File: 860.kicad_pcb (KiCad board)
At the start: 4 copper layers, 38 x 106 mm, 150 parts, among them J1 PJ301B, J2 PJ301B, J3 PJ301B, J4 PJ301B, J5 PJ301B, J6 PJ301B, P1 CONN_02X05, Q1 BCM857BS, Q2 BCM857BS, Q3 J112, Q4 J112, Q5 J112, Q6 J112, SW1 B3F-1050, U1 TL072-, U10 CD4027, U11 CD40106, U12 TS321, U13 TS321, U2 TL072-, U3 TL072-, U4 TL072-, U5 LM13700, U6 LM13700, U7 LM13700, U8 DG409, U9 CD4052

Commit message: routed, silk screen adjusted
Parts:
- C18, C25, C6, C7: footprint MyModules:SM0805-HAND -> MyModules:SM0805-HAND-C
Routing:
- net GND: track 88.8 -> 92.7 mm, vias 24 -> 26
- net Net-(J4-Pad3): track 32.3 -> 35.5 mm
- net Net-(U1-Pad5): track 43.1 -> 45.9 mm
- net Net-(U10-Pad1): track 72.7 -> 75.2 mm
- net Net-(Q3-Pad1): track 55.1 -> 53.7 mm
- net Net-(R48-Pad1): track 26.9 -> 28.0 mm
- net Net-(J1-Pad3): track 35.0 -> 34.0 mm
- net -12V: track 290.8 -> 291.7 mm
- net Net-(C11-Pad1): track 54.5 -> 55.3 mm
- net Net-(R31-Pad1): track 2.08 -> 2.60 mm
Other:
- rule pad_to_mask_clearance: 0.2 -> 0.05

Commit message: getting pretty close to done
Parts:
- added G***: LOGO, LOGO, B.Cu at (122.2, 127.8)
- added REF***: OSHW-Symbol_6.7x6mm_SilkScreen, Symbols:OSHW-Symbol_6.7x6mm_SilkScreen, B.Cu at (135.4, 41.9)
- moved D6 0.20 mm to (121.3, 106.5)
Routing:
- net -12V: vias 17 -> 16
- added copper zone on B.Cu, net -12V
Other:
- board text added: "860"
- board text added: "FREQ"
- board text added: "RES"
- board text added: "r1 11/17"
- board text added: "system80.net"

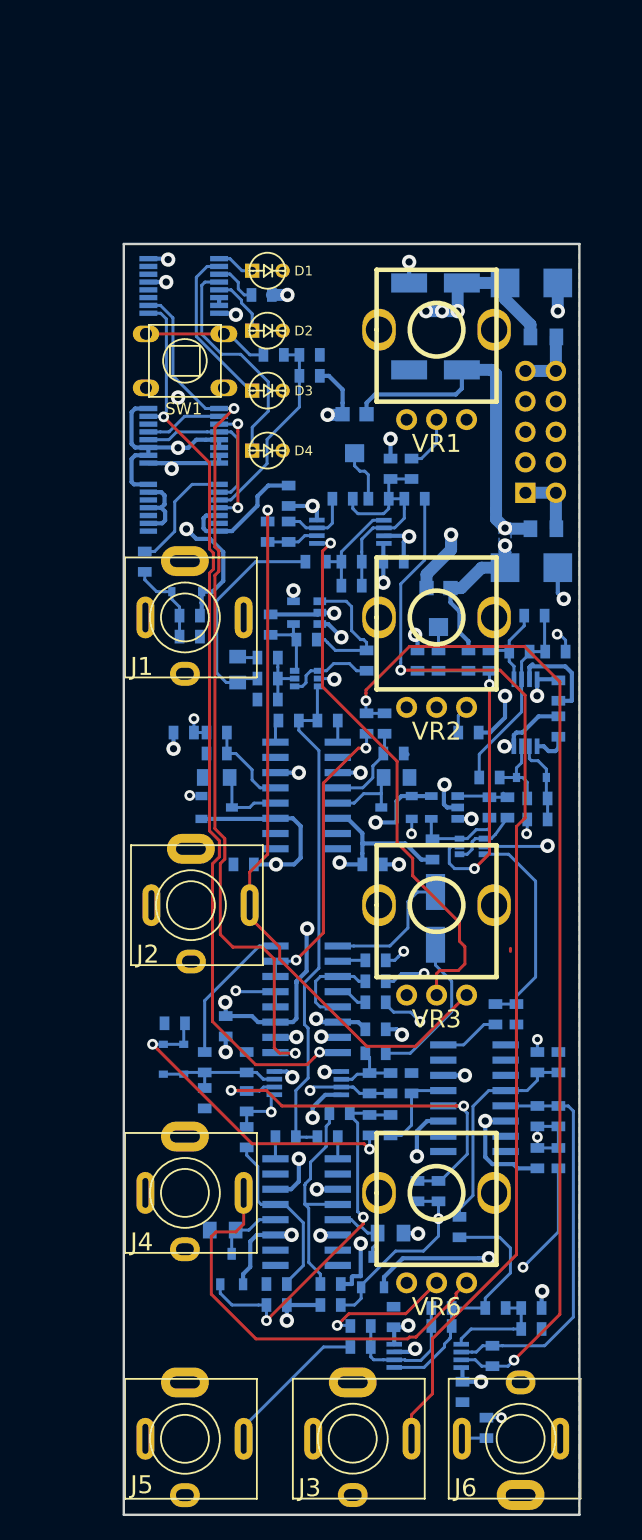
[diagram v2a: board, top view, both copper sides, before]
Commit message: front component adjustments to jive with panel template
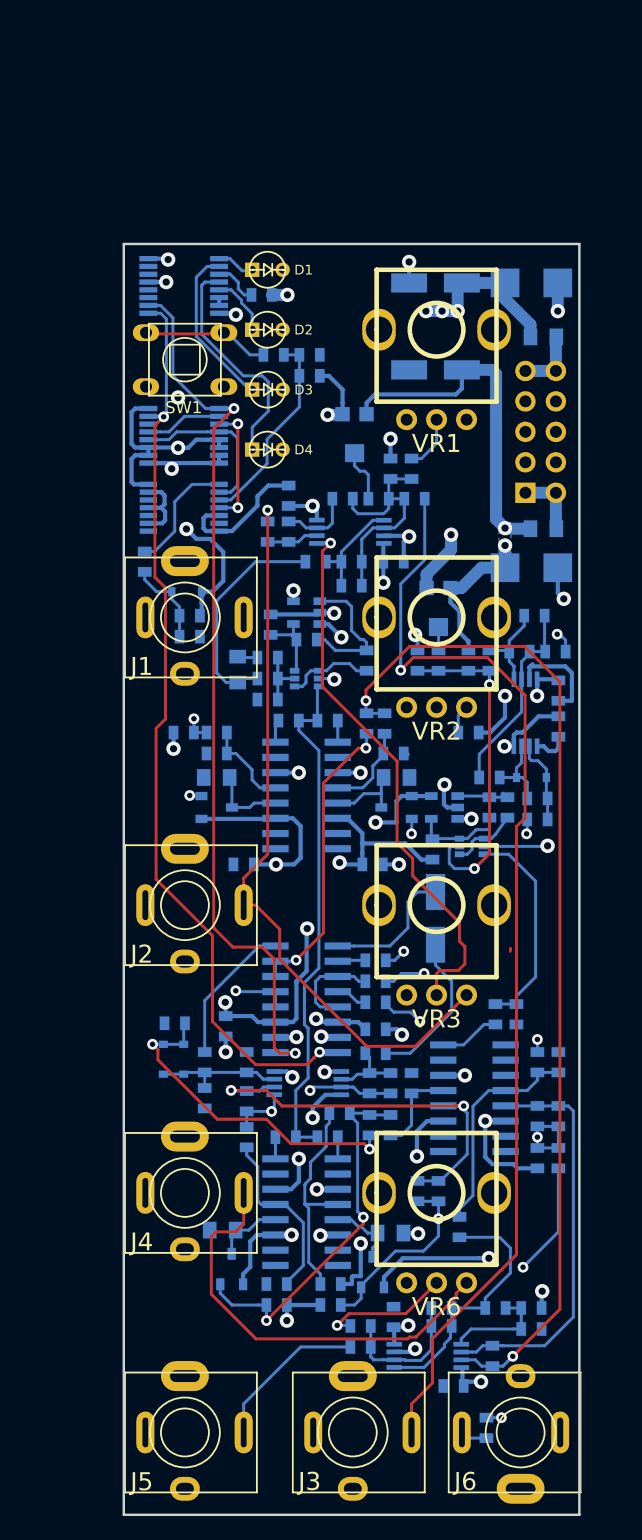
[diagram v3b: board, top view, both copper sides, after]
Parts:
- moved C14 0.90 mm to (145.5, 133.8), turned to 180 degrees
- moved J5 0.53 mm to (123.1, 137.6)
- moved J3 0.52 mm to (137.1, 137.6)
- moved J6 0.52 mm to (151.1, 137.6)
- moved J2 0.50 mm to (123.1, 93.7)
- moved SW1 0.10 mm to (123.1, 48.1)
- moved D1 0.08 mm to (130.0, 40.6)
- moved D2 0.08 mm to (130.0, 45.6)
- moved D3 0.08 mm to (130.0, 50.6)
- moved D4 0.08 mm to (130.0, 55.6)
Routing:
- net Net-(J2-Pad3): track 60.4 -> 62.4 mm
- net Net-(J5-Pad3): track 12.7 -> 13.8 mm
- net Net-(J3-Pad3): track 92.3 -> 93.2 mm
- net -12V: track 291.7 -> 292.4 mm
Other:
- board text added: "-12V"
- board text added: "r1.1 02/18"
- board text removed: "r1 11/17"

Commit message: tweaked routing to improve ground plane
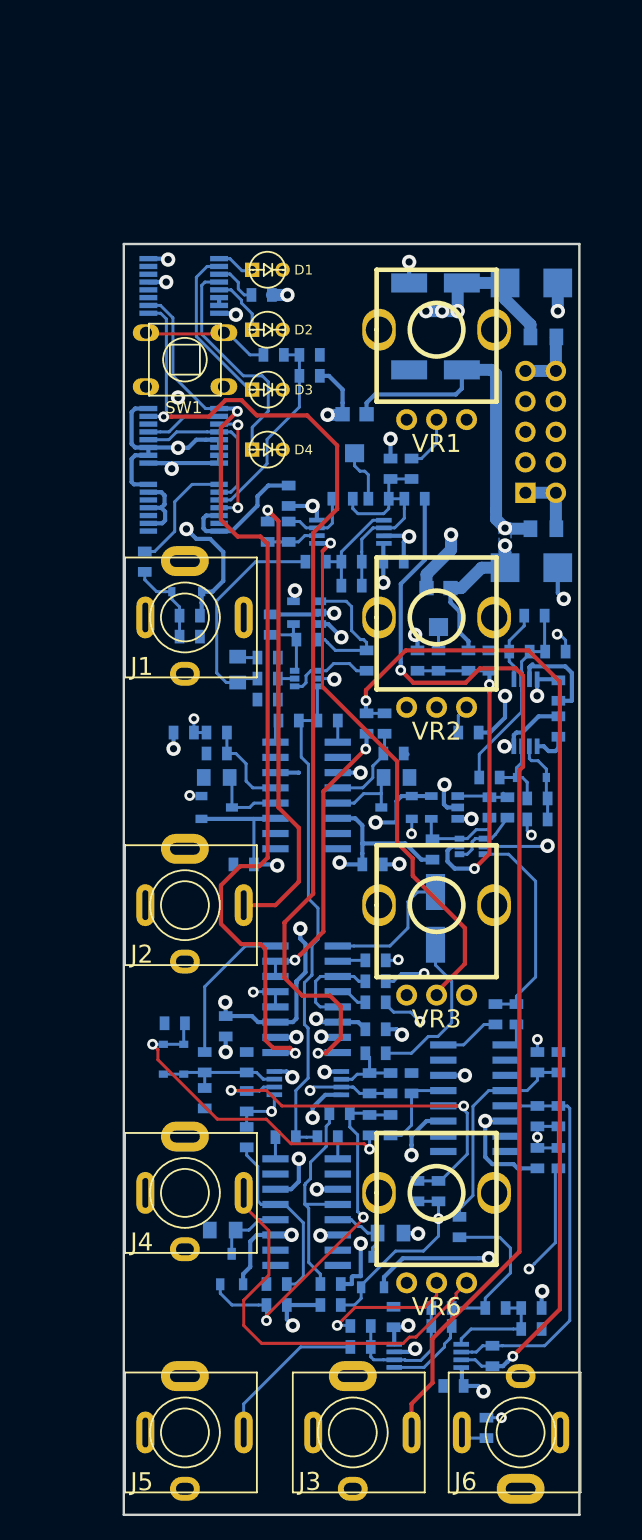
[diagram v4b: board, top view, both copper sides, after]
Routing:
- net Net-(U10-Pad15): track 77.0 -> 86.5 mm
- net Net-(U10-Pad1): track 74.7 -> 79.3 mm
- net -12V: track 292.4 -> 294.7 mm
- net Net-(J1-Pad3): track 34.0 -> 36.0 mm
- net +12V: track 352.8 -> 354.8 mm
- net OUT2A: track 58.8 -> 57.1 mm
- net Net-(R48-Pad1): track 27.8 -> 26.3 mm
- net Net-(J4-Pad3): track 35.5 -> 34.3 mm
- net Net-(U1-Pad5): track 45.9 -> 45.0 mm
- net Net-(J3-Pad3): track 93.2 -> 94.0 mm
- net SWX1: track 12.1 -> 12.8 mm
- net Net-(R7-Pad2): track 10.9 -> 11.5 mm
- net Net-(C10-Pad1): track 13.1 -> 13.6 mm
- net GND: vias 26 -> 25

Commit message: fixed hardware placement to match panel mechanical, moving power header
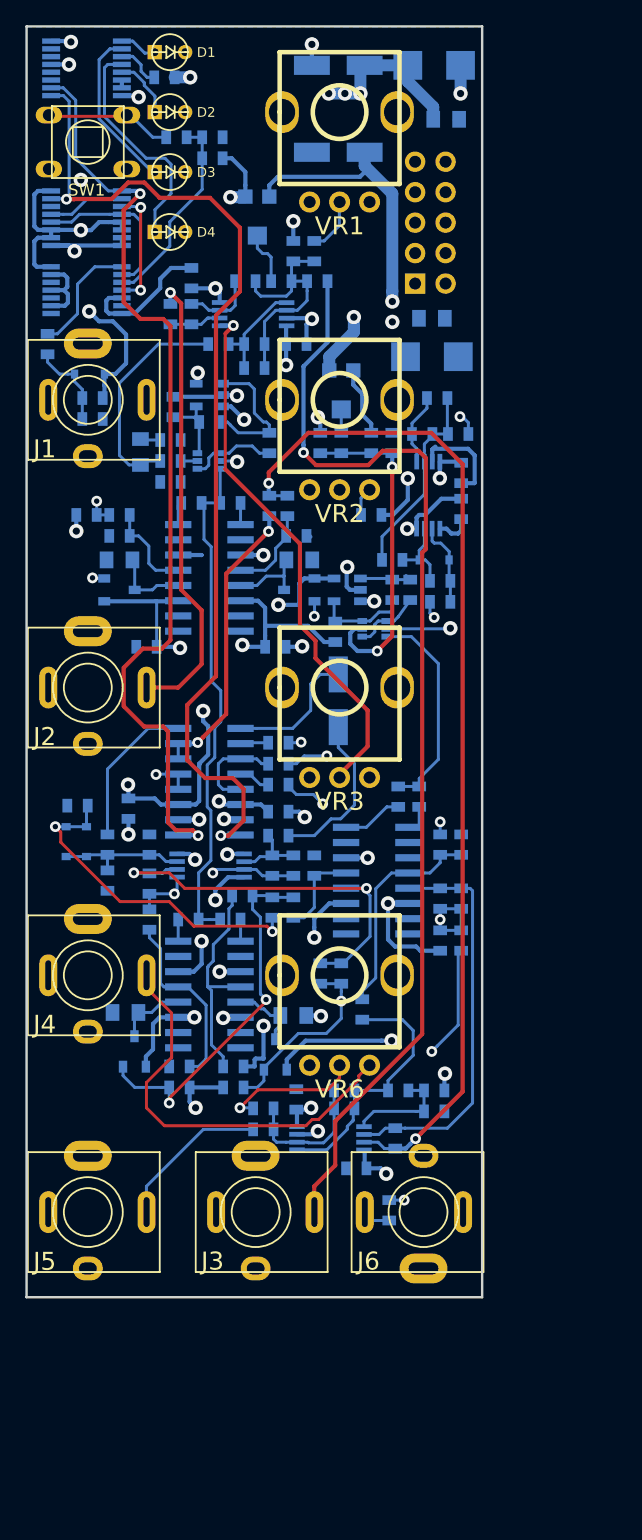
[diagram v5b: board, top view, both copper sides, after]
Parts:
- moved J3 20.1 mm to (129.0, 119.2)
- moved J5 20.1 mm to (115.0, 119.2)
- moved J6 20.1 mm to (143.0, 119.2)
- moved D1 19.9 mm to (121.8, 22.5)
- moved D2 19.9 mm to (121.8, 27.5)
- moved D3 19.9 mm to (121.8, 32.5)
- moved D4 19.9 mm to (121.8, 37.5)
- moved C1 19.9 mm to (136.4, 110.6)
- moved C10 19.9 mm to (135.9, 76.6)
- moved C11 19.9 mm to (132.1, 90.3)
- moved C14 19.9 mm to (137.4, 115.6)
- moved C15 19.9 mm to (132.4, 109.8)
- moved C19 19.9 mm to (130.9, 85.8)
- moved C2 19.9 mm to (140.4, 67.3)
- moved C25 19.9 mm to (132.1, 102.8)
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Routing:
- net -12V: track 294.7 -> 282.3 mm
- net Net-(F1-Pad2): track 5.56 -> 0.00 mm
- net Net-(F2-Pad2): track 5.40 -> 0.06 mm
- net GND: track 92.7 -> 89.9 mm, vias 25 -> 24
- removed copper zone on B.Cu, net -12V
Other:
- board text added: "r1.2 05/19"
- board text removed: "r1.1 02/18"

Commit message: updated 0603 footprints for production, new hole centres for aligning with panel holes
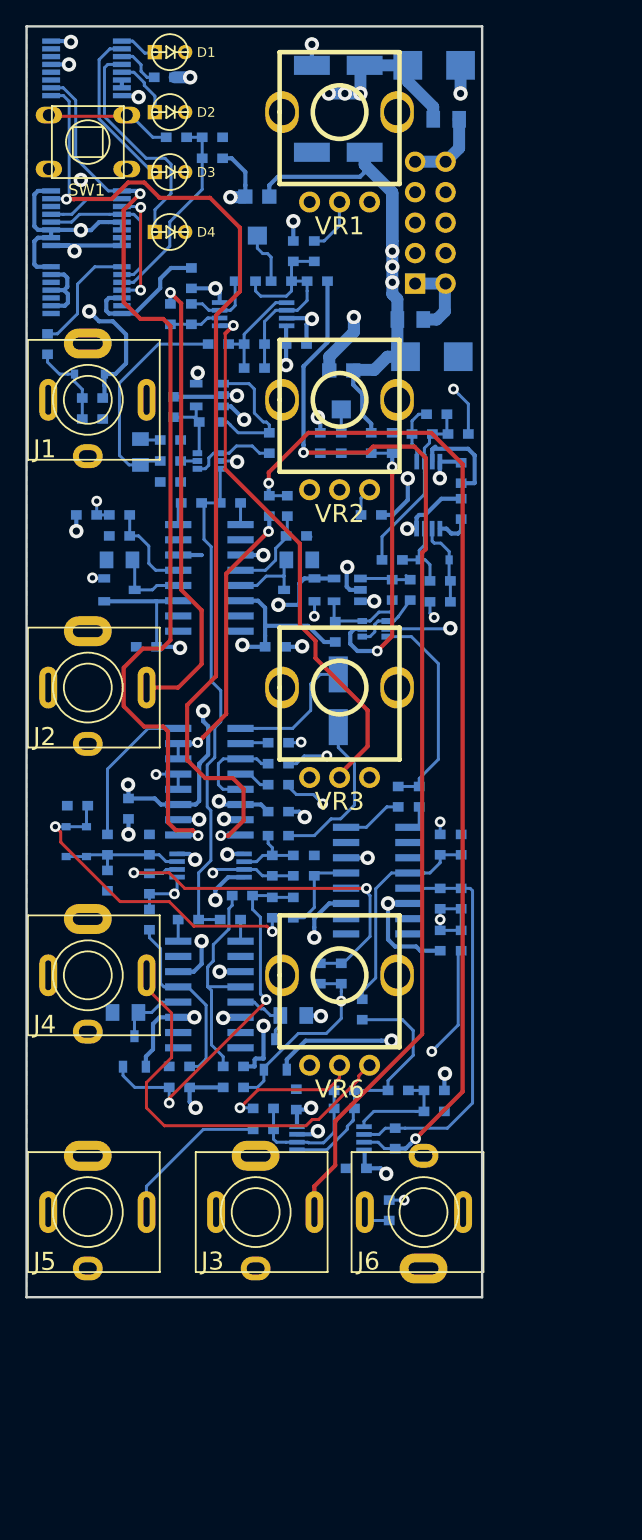
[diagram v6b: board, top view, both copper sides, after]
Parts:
- C1, C11, C12, C13, C14, C15, C16, C17, C19, C2, C20, C21, C22, C26, C27, C28, C29, C3, C4, C5, C8, C9: footprint MyModules:SM0603-C-JRL -> MyModules:SM0603-C-MURATA
- R1, R10, R11, R12, R13, R14, R15, R16, R17, R18, R2, R20, R21, R22, R23, R24, R25, R26, R27, R28, R29, R3, R30, R31, R32, R33, R34, R35, R36, R37, R38, R39, R4, R40, R41, R42, R43, R44, R45, R46, R47, R48, R49, R5, R50, R51, R52, R53, R54, R55, R56, R57, R58, R59, R6, R60, R61, R62, R63, R64, R65, R68, R69, R7, R70, R71, R72, R73, R74, R75, R76, R77, R78, R8, R9: footprint MyModules:SM0603-R-JRL -> MyModules:SM0603-R-YAGEO
- moved F1 1.80 mm to (141.9, 44.8)
- moved C28 1.35 mm to (144.1, 52.7)
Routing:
- net -12V: track 282.3 -> 301.2 mm, vias 16 -> 17
- net Net-(F1-Pad2): track 0.00 -> 6.97 mm
- net Net-(F2-Pad2): track 0.06 -> 6.60 mm
- net Net-(R2-Pad2): track 15.8 -> 17.3 mm
- net Net-(C28-Pad2): track 16.6 -> 15.5 mm
- net Net-(C28-Pad1): track 7.68 -> 6.70 mm
- net Net-(J3-Pad3): track 94.0 -> 93.4 mm
- net Net-(C11-Pad2): track 5.58 -> 6.12 mm

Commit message: added backplane and corresponding snap holes
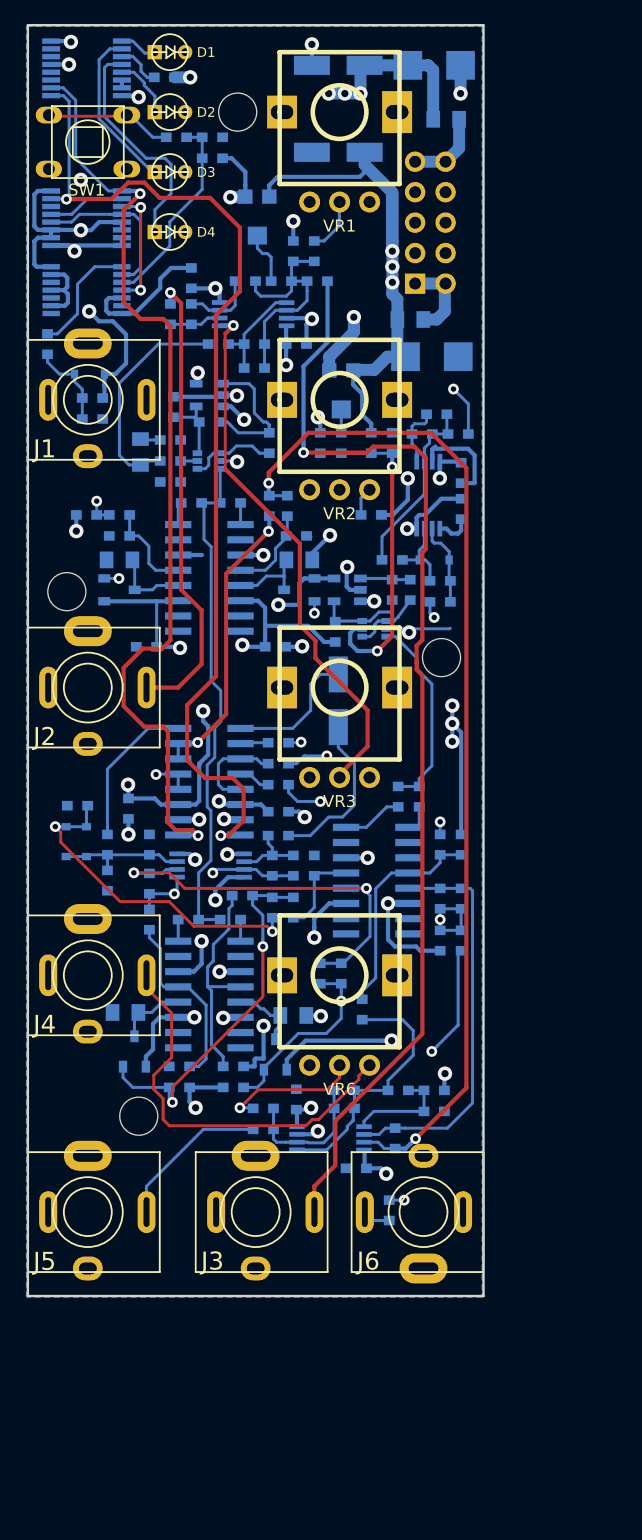
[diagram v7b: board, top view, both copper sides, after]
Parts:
- added G***: LOGO, LOGO, B.Cu at (125.2, 75.0)
- added SNAP-HOLE-0.125-INCH: VAL**, MyModules:SNAP_HOLE_0.125_INCH, F.Cu at (144.5, 73.0)
- added SNAP-HOLE-0.125-INCH: VAL**, MyModules:SNAP_HOLE_0.125_INCH, F.Cu at (119.2, 111.2)
- added SNAP-HOLE-0.125-INCH: VAL**, MyModules:SNAP_HOLE_0.125_INCH, F.Cu at (113.2, 67.5)
- added SNAP-HOLE-0.125-INCH: VAL**, MyModules:SNAP_HOLE_0.125_INCH, F.Cu at (127.5, 27.5)
- VR1, VR2, VR3, VR6: footprint MyModules:RD901F-ALPHA-POT-T18 -> MyModules:RD901F-40-ALPHA-POT-T18
- moved G*** 0.46 mm to (114.0, 109.2)
- moved REF*** 0.33 mm to (127.5, 23.5)
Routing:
- net GND: track 89.9 -> 107.2 mm, vias 24 -> 28
- net Net-(C3-Pad1): track 66.6 -> 64.1 mm
- net Net-(Q3-Pad1): track 53.7 -> 52.1 mm
- net RES_CTRL: track 17.9 -> 16.7 mm
- net -12V: track 301.2 -> 302.2 mm
- net Net-(J4-Pad3): track 34.3 -> 33.5 mm
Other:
- board text removed: "860"

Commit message: working on backplane, DRC done on 860 PCB
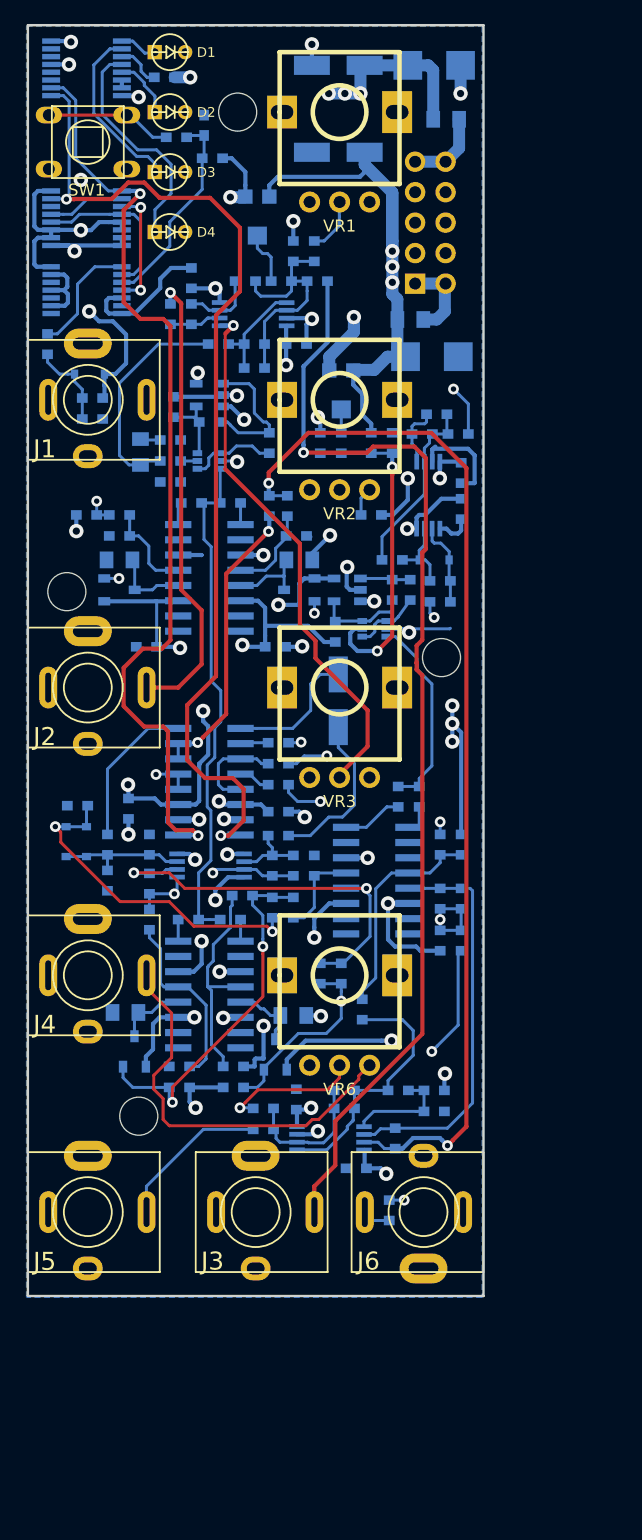
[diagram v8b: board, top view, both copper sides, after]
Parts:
- added G***: LOGO, w_logo:Logo_silk_CE_5x3.6mm, B.Cu at (129.7, 119.2)
- added G***: LOGO, w_logo:Logo_silk_ROHS_5x2.8mm, B.Cu at (122.7, 121.3)
- added REF***: WEEE-Logo_4.2x6mm_SilkScreen, Symbols:WEEE-Logo_4.2x6mm_SilkScreen, B.Cu at (122.8, 116.5)
- moved C21 1.21 mm to (124.7, 28.6), turned to 90 degrees
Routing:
- net Net-(R26-Pad1): track 85.1 -> 87.5 mm
- net Net-(D3-Pad2): track 13.7 -> 14.6 mm
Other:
- board text added: "r1.2 06/19"
- board text removed: "r1.2 05/19"
